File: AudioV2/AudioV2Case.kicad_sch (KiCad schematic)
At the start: 0 parts

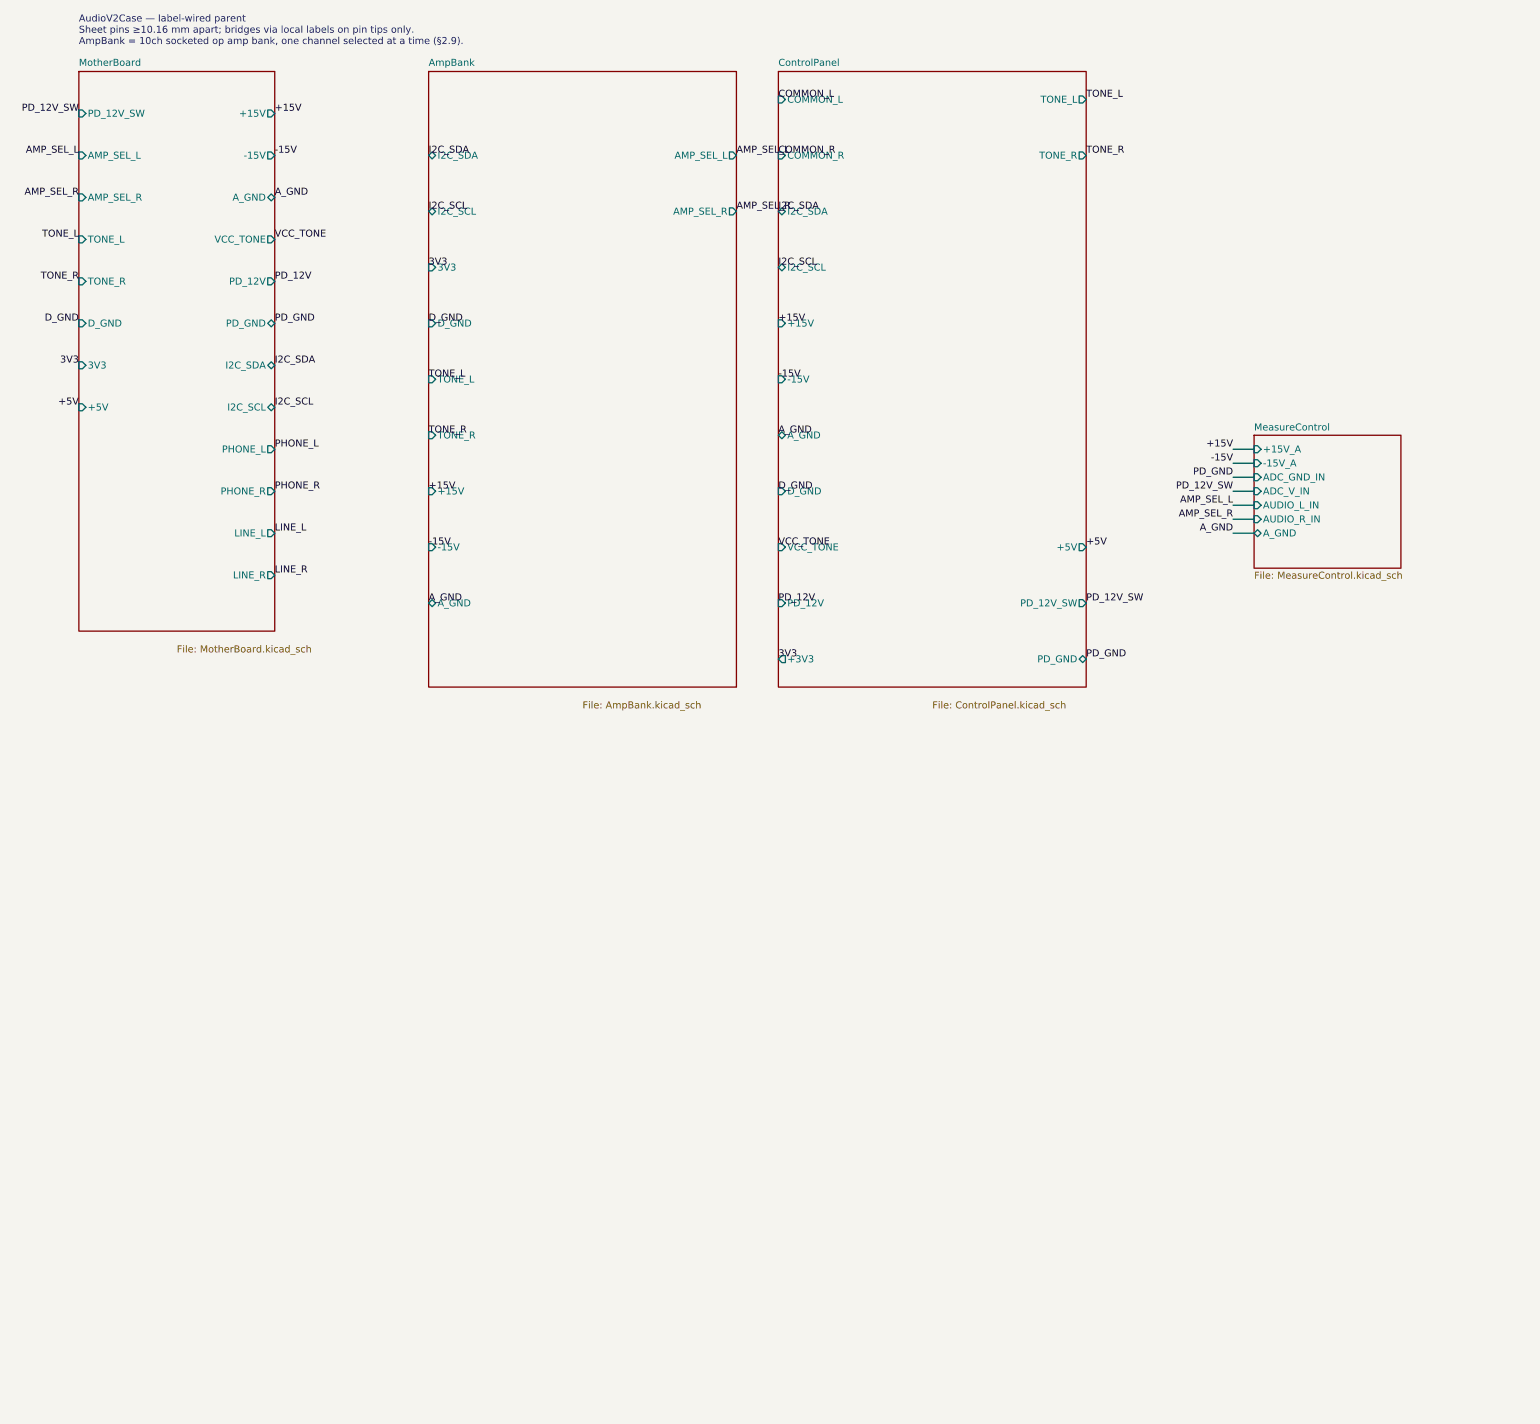
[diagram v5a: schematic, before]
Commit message: AudioV2: 娘基板を 5ch×2枚へ（B3a スイッチ版 / B3b リレー版）
D19 のとおり 5ch×2枚。D9 のとおり**スロット1にスイッチ版・スロット2にリレー版**を
挿した状態を親に組んだ。両版が同じ AMP_SEL_L/R バスにぶら下がるので、
同一セッション内で切替素子だけを比較できる。AmpChannel は D22 で共通化済み。

新規 build_daughter.py が2種を1つの定義から生成する。結線はピン先のラベルで、
ピン座標は KiCad のシンボルから直読み。

  AmpBankSwitch  部品15 / AmpChannel×5 / TMUX7612×3（12スイッチ中10使用）
  AmpBankRelay   部品15 / AmpChannel×5 / AZ850P2-5×5 / ドライバ×2

リレー版で記録から拾って設計に反映したこと:
- **ドライバは ULN2803 ではなく TBD62083APG**（ピン互換のドロップイン）。
  §2.7-3 で「ダーリントンが約1V落とすので 40℃ 超で AZ850 の Must Operate 3.75V を
  満たさない」と検算済みだった。DMOS なら RON 3.25Ω max で 40mA 時 0.13V
- **ドライバは2個要る**。5ch×2コイル=10本 > 8ch。4ch/枚なら1個で済んでいた
  （5ch/枚を選んだぶんのコスト）
- AZ850 のピン割当は削除済み RelayBoard から復元（コイル 1-5 / 10-6、接点 3-2/4 と 8-9/7）
- **接点は ch 出力を COM に、共通バスを NO に**入れる。逆にすると非選択 ch が
  バスを自分の反対接点へ落とす
- FP は v1 実績の Relay_THT:Relay_DPDT_FRT5

検証（ネットリスト）:
- 部品 369 個すべてユニーク。3階層（親→娘基板×2→ch×5）が成立
- 番地: スイッチ版 A0/A1/A2 = D_GND → **0x20**、リレー版 A0=3V3 → **0x21**（D21）
- リレー版の制御チェーン: MCP GPA2 → ドライバ in5 → out14 → K303 の SET コイル
- AMP_SEL_R に両版が同居（TMUX 6ピン ＋ リレー 5接点）
- GND_COIL が1本に統合（母板の NetTie ＋ リレー版ドライバの GND ＋ コネクタ）

ERC 51 -> 49。

途中で3件やらかして直した:
1. **番地が両スロットで同じネットに合流していた。** 娘基板の階層ピン名を親でも
   そのまま使ったため。スロットごとに D_GND/3V3 へ差し替える PARENT_NET を追加
2. **GND_COIL が母板内とルートで別ネットだった。** 親にシートピンを足すだけでは
   繋がらず、母板シート側にも階層ラベルが要る
3. リレーの FP 名を勝手に作っていた（Relay_DPDT_Zettler_AZ850P は存在しない）。
   ERC の footprint_link_issues で気付いた

旧 AmpBank.kicad_sch は legacy/ へ凍結。

Co-Authored-By: Claude Opus 5 <noreply@anthropic.com>
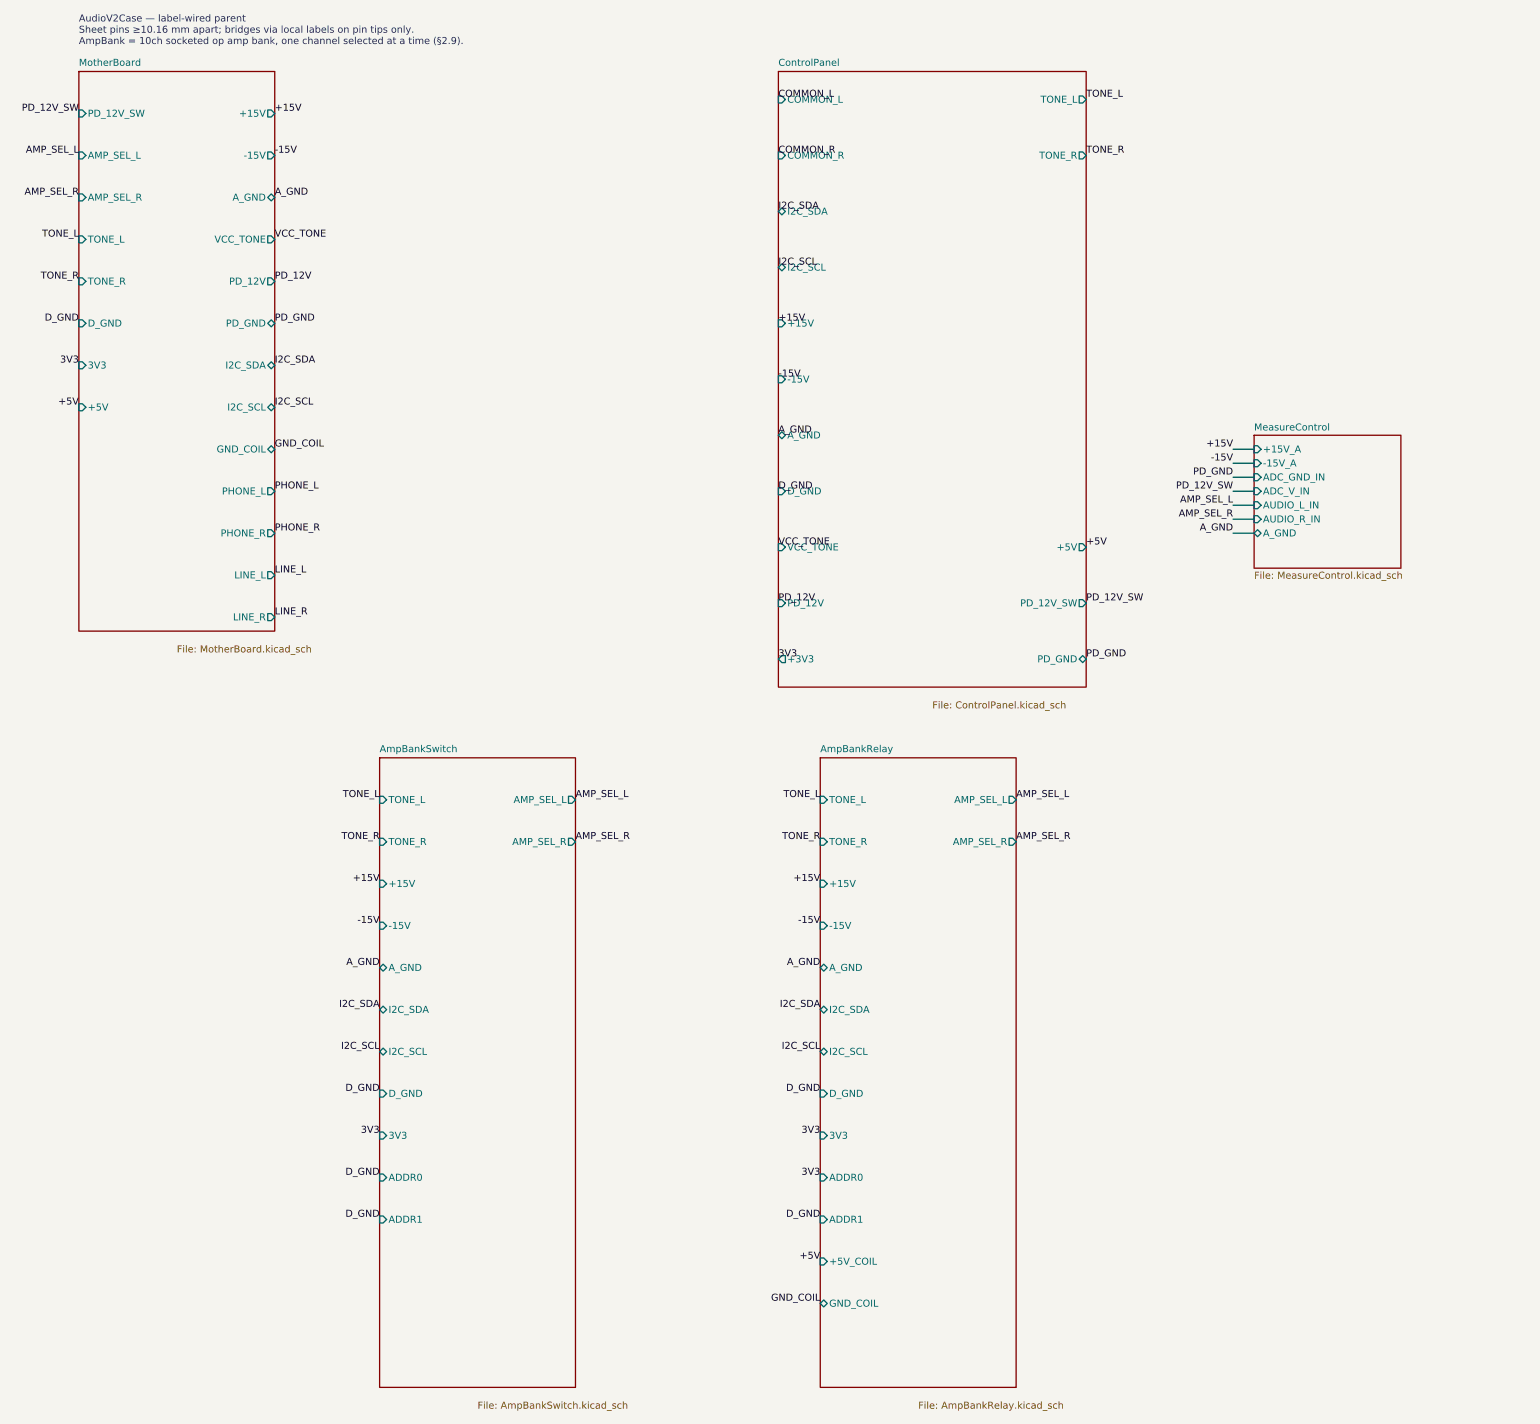
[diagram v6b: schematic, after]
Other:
- sheet AmpBank renamed AmpBankSwitch
- added sheet AmpBankRelay (AmpBankRelay.kicad_sch)
- sheet AmpBankSwitch: file AmpBank.kicad_sch -> AmpBankSwitch.kicad_sch
- sheet AmpBankSwitch ports: added ADDR0, ADDR1; removed none
- sheet MotherBoard ports: added GND_COIL; removed none

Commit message: AudioV2: B4'-1/B4'-2 完了。ControlPanel を解体し、シートは4枚になった
B4'-1（UI と I2C マスタを計測基板へ / D27）:
- MeasureControl に MCP23017(U1610, 0x22)＋100nF、ENC1601-1603、DEST LED×2＋1k、
  OLED、I2C プルアップ 4.7k×2、DEST センスラダー（SW1601＋抵抗4本）を追加
- 計測 Pico の空きピンへ直付け: GPIO20/21 = I2C_SDA/SCL、GPIO26(ADC0) = DEST_ADC
- **系の 3V3 は A1602.36（計測 Pico の 3V3_OUT）から**。+3V3_A（LT1763）は
  PCM1804・水晶・監視ICの清浄レールなので触っていない（D27）
- 階層ピンに I2C_SDA / I2C_SCL / 3V3 / D_GND を追加

B4'-2（PT2314 と +5V を母板へ、ControlPanel 廃止）:
- 残り23部品（PT2314＋周辺20点・BP5293-50・パネル PWR SW・12V LED）を母板へ統合
- VCC_TONE と PD_12V は作る側と使う側の両方が母板に収まったので階層ピンから外した
- 母板の階層ピンは 21 本。TONE_L/R と +5V は input -> output へ（母板が作る側になった）
- 母板の用紙を A3 -> A2 へ

検証:
- 部品 370 個すべてユニーク。シートは MotherBoard / MeasureControl /
  AmpBankSwitch / AmpBankRelay の4枚（ControlPanel は消滅、U401 も消えた）
- /3V3 の駆動は A1602.36、/+5V の駆動は U403.3（BP5293、母板）
- /VCC_TONE と /PD_12V はルートから消えて母板内部のネットになった
- **ERC 49 -> 29**。残る multiple_net_names 1件は 3V3/PICO_3V3 の意図的な別名

途中で3件やらかして直した:
1. **既存の配線の上に新部品を重ねた。** MeasureControl の使用範囲を要素の
   アンカーだけで測って y<=233.7 と誤ったが、**ワイヤの端点まで入れると y=315**
   だった。空きを測るときはワイヤの端点も入れること
2. **親で同じネットに2つ名前が付いた。** 元の7ピンはユーザーが (234.95,y) の
   ラベル＋ワイヤで結線済みなのに、ピン位置にもラベルを重ねたため。
   増えた4本にだけ置くようにした
3. **計測 Pico の空きピンに残っていた no_connect** を外さずにラベルを乗せて
   no_connect_connected になった

Co-Authored-By: Claude Opus 5 <noreply@anthropic.com>
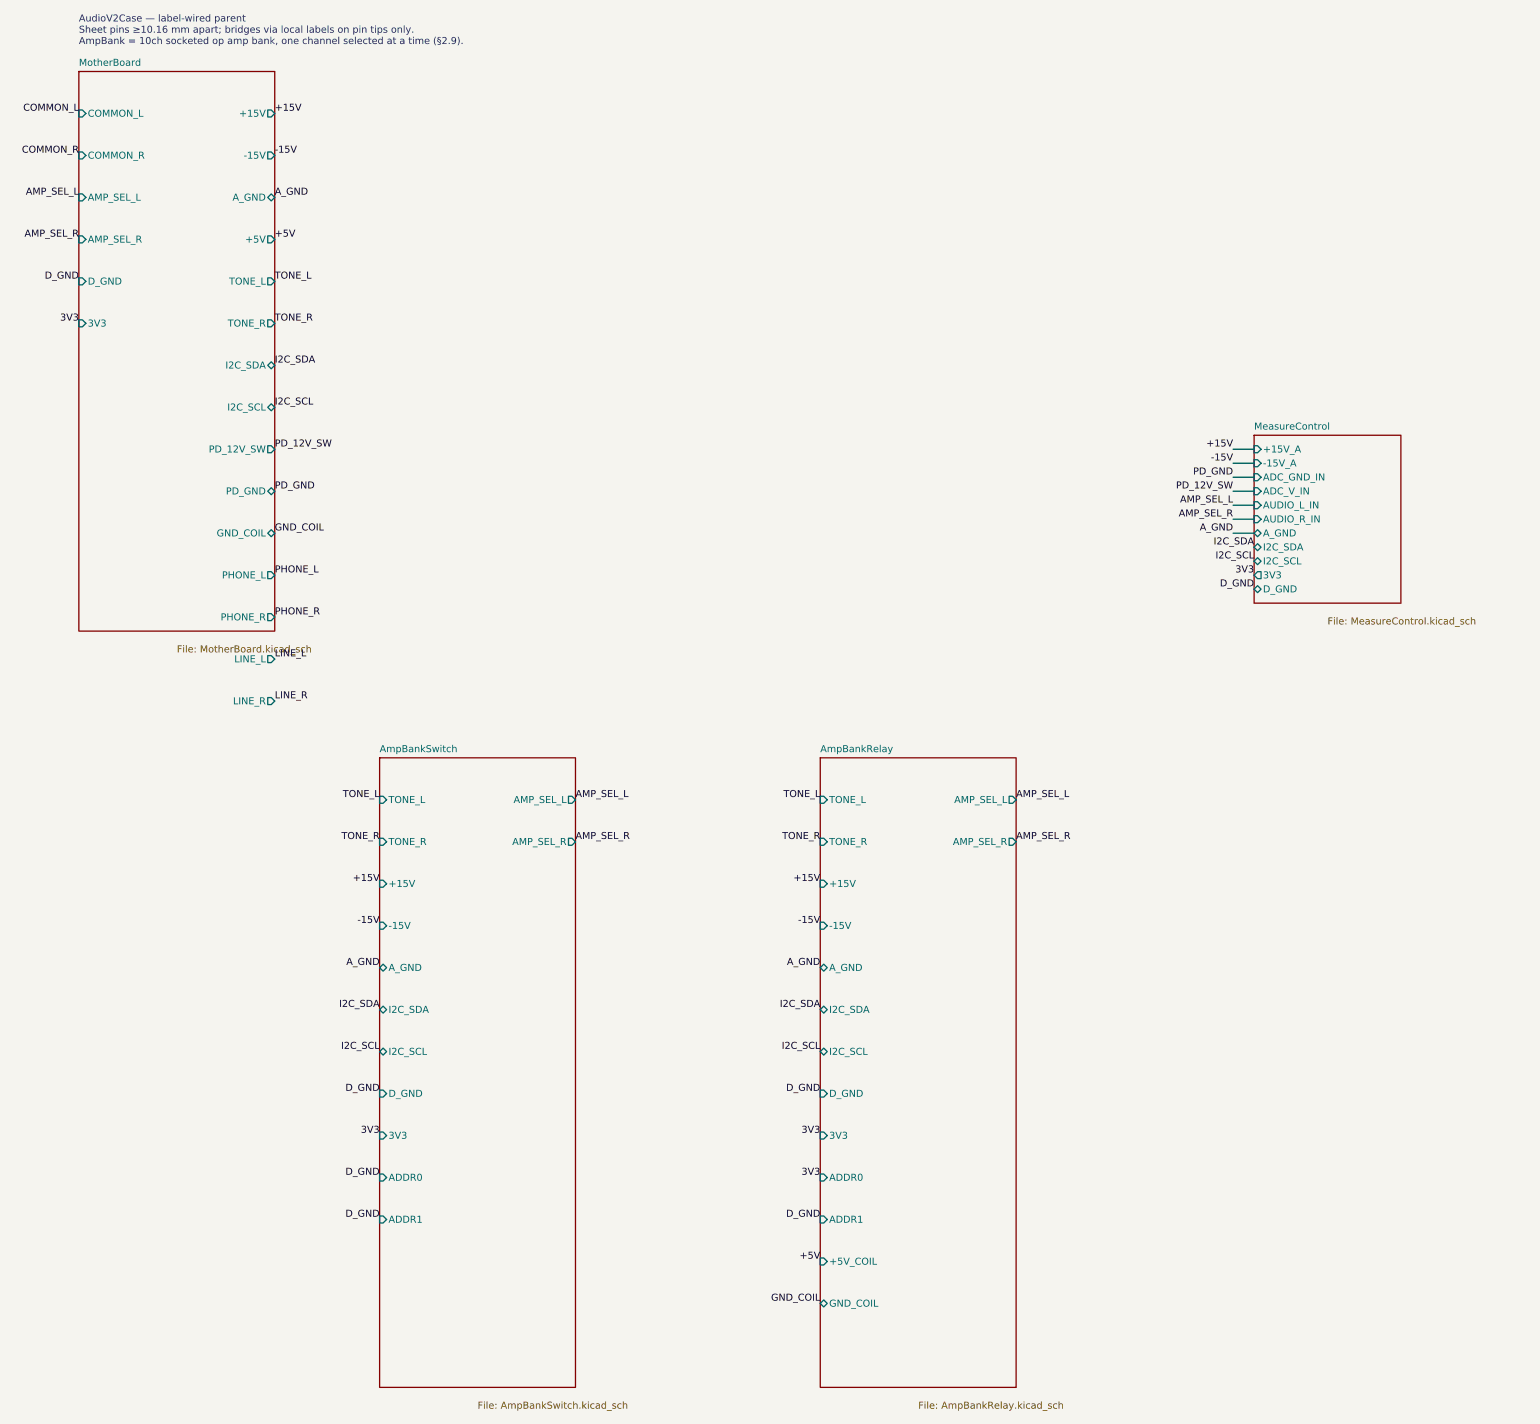
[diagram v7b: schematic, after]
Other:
- removed sheet ControlPanel
- sheet MeasureControl ports: added 3V3, D_GND, I2C_SCL, I2C_SDA; removed none
- sheet MotherBoard ports: added COMMON_L, COMMON_R; removed PD_12V, VCC_TONE
